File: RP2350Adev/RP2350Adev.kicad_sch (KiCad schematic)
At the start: 43 parts, among them J1 USB4105-GF-A, J2 LEFT, J3 DEBUG, J4 RIGHT, U1 W25Q32JV, U2 RP2350A, U3 MCP1702T-3302E_CB, X1 IQXO-791

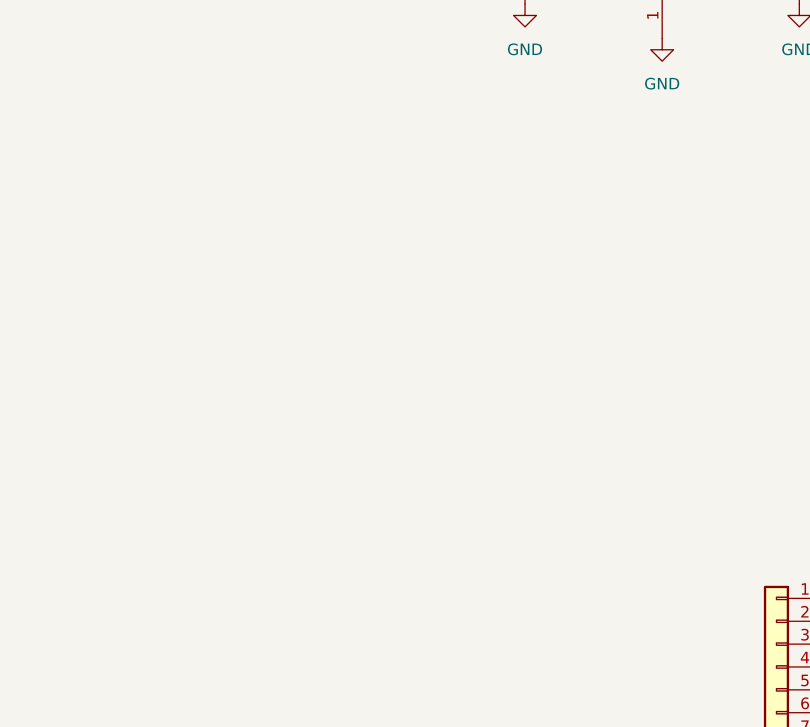
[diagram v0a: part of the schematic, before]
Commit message: add nrf70
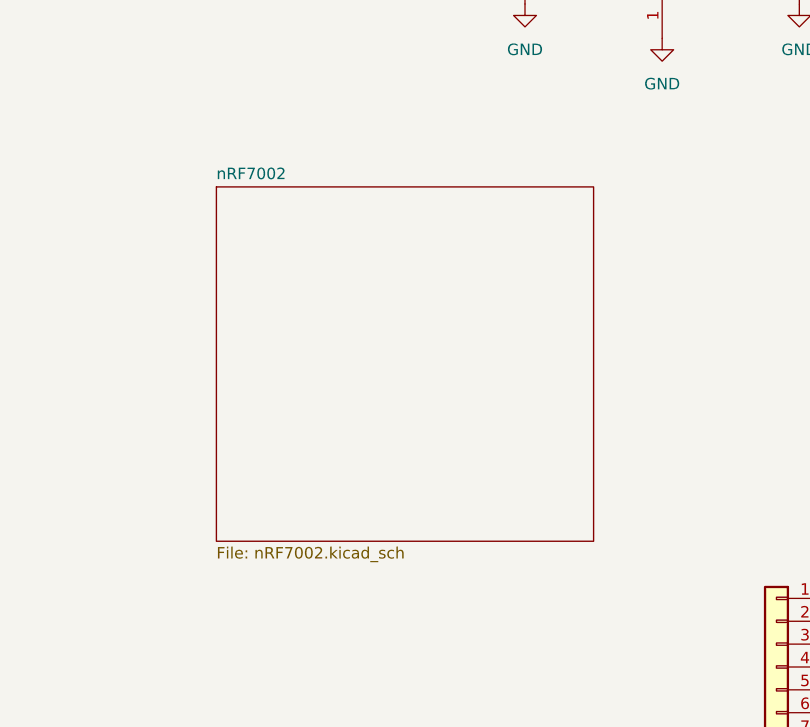
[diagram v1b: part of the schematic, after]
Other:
- added sheet nRF7002 (nRF7002.kicad_sch)
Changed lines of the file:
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@@
+		)
+	)
+	(sheet
+		(at 204.47 64.77)
+		(size 41.91 39.37)
+		(exclude_from_sim no)
+		(in_bom yes)
+		(on_board yes)
+		(dnp no)
+		(fields_autoplaced yes)
+		(stroke
+			(width 0.1524)
+			(type solid)
+		)
+		(fill
+			(color 0 0 0 0.0000)
+		)
+		(property "Sheetname" "nRF7002"
+			(at 204.47 64.0584 0)
+			(effects
+				(font
+					(size 1.27 1.27)
+				)
+				(justify left bottom)
+			)
+		)
+		(property "Sheetfile" "nRF7002.kicad_sch"
+			(at 204.47 104.7246 0)
+			(effects
+				(font
+					(size 1.27 1.27)
+				)
+				(justify left top)
+			)
+		)
+		(instances
+			(project "RP2350Adev"
+				(path "/4930e8a3-0a58-4861-9c4c-0d8b2139987a"
+					(page "2")
+				)
+			)
 		)
 	)

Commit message: Muxful beginnings
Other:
- moved on the sheet: C16, C17, D3, J2, R12, U3

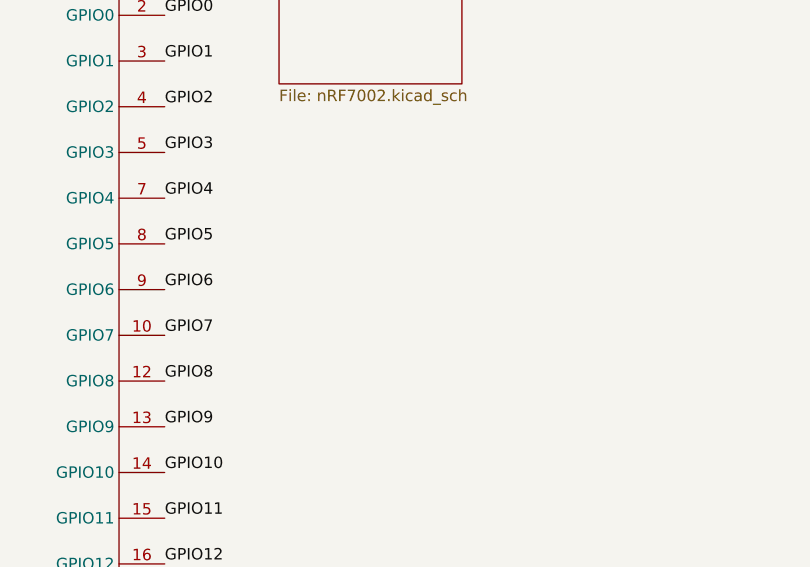
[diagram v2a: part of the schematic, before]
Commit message: link hierarchical sheet and switch from QSPI to SPI
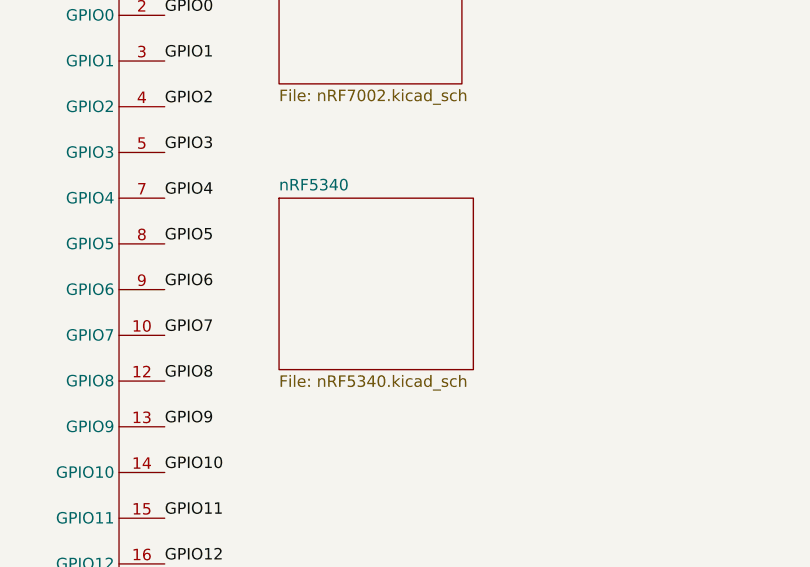
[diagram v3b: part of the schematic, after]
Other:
- added sheet nRF5340 (nRF5340.kicad_sch)
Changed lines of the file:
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@@
+		)
+	)
+	(sheet
+		(at 186.69 53.34)
+		(size 21.59 19.05)
+		(exclude_from_sim no)
+		(in_bom yes)
+		(on_board yes)
+		(dnp no)
+		(fields_autoplaced yes)
+		(stroke
+			(width 0.1524)
+			(type solid)
+		)
+		(fill
+			(color 0 0 0 0.0000)
+		)
+		(property "Sheetname" "nRF5340"
+			(at 186.69 52.6284 0)
+			(effects
+				(font
+					(size 1.27 1.27)
+				)
+				(justify left bottom)
+			)
+		)
+		(property "Sheetfile" "nRF5340.kicad_sch"
+			(at 186.69 72.9746 0)
+			(effects
+				(font
+					(size 1.27 1.27)
+				)
+				(justify left top)
+			)
+		)
+		(instances
+			(project "RP2350Adev"
+				(path "/4930e8a3-0a58-4861-9c4c-0d8b2139987a"
+					(page "3")
+				)
+			)
 		)
 	)

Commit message: Muxful Developings
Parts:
- removed J1: USB4105-GF-A, Eclectronics:USB4105-GF-A, symbol Eclectronics:USB4105-GF-A
- removed R3, R4: 5.1K, Resistor_SMD:R_0402_1005Metric, symbol Device:R
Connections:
- no-connect marks 4 -> 2

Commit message: Combine subsheets
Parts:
- removed J2: LEFT, Connector_PinHeader_2.54mm:PinHeader_1x20_P2.54mm_Vertical, symbol Connector_Generic:Conn_01x20
- removed J4: RIGHT, Connector_PinHeader_2.54mm:PinHeader_1x20_P2.54mm_Vertical, symbol Connector_Generic:Conn_01x20
- added J5: UART, Connector_PinHeader_1.00mm:PinHeader_1x03_P1.00mm_Vertical, symbol Connector_Generic:Conn_01x03
- renumbered C16 to C26, C1 to C27, C17 to C28, C2 to C29, C3 to C30, C4 to C31, C5 to C32, C6 to C33, C7 to C34, C8 to C35, C9 to C36, C10 to C37, C11 to C38, C12 to C39, C13 to C40, C14 to C41, C15 to C42, D3 to D2, D1 to D3, D2 to D4, J3 to J6, L1 to L7, R12 to R10, R5 to R11, R6 to R12, R7 to R13, R8 to R14, R9 to R15, R10 to R16, R11 to R17, R1 to R8, R2 to R9, U3 to U5, U1 to U6, U2 to U7, X1 to X4
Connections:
- net GND: now also J5.3 (Pin_3)
- net D1+: now reaches R12.1
- net D1-: now reaches R11.1
- net GPIO0: no longer names the net of U7.2 (GPIO0)
- net GPIO0: now also J5.1 (Pin_1)
- net GPIO1: no longer names the net of U7.3 (GPIO1)
- net GPIO1: now also J5.2 (Pin_2)
- net GPIO10 renamed MUX2_S
- net GPIO11 renamed MUX2_OE
- net GPIO12 renamed MUX1_S1
- net GPIO13 renamed MUX1_S0
- net GPIO14 renamed D2+
- net GPIO15 renamed D2-
- net GPIO2 renamed SPI_CLK
- net GPIO3 renamed SPI_MOSI
- net GPIO4 renamed SPI_MISO
- net GPIO5 renamed SPI_SS
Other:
- removed sheet nRF5340
- removed sheet nRF7002
- company: Olin College -> (none)
- title: RP2350A Development Board -> (none)
- moved on the sheet: J6

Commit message: Layout Assembly Attempt (Components not being transferred as expected, major issues)
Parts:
- renumbered C26 to C36, C27 to C37, C28 to C38, C29 to C39, C30 to C40, C31 to C41, C32 to C42, C33 to C43, C34 to C44, C35 to C45, C36 to C46, C37 to C47, C38 to C48, C39 to C49, C40 to C50, C41 to C51, C42 to C52
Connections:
- no-connect marks 2 -> 16

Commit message: Combine subcircuits
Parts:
- J401: renamed from J5; footprint Connector_PinHeader_1.00mm:PinHeader_1x03_P1.00mm_Vertical -> Connector_PinHeader_2.54mm:PinHeader_1x03_P2.54mm_Vertical
- J402: renamed from J6; footprint Connector_PinHeader_1.00mm:PinHeader_1x03_P1.00mm_Vertical -> Connector_PinHeader_2.54mm:PinHeader_1x03_P2.54mm_Vertical
- U401: renamed from U5; footprint Parts:SOT95P255X145-3N -> Package_TO_SOT_SMD:SOT-23
- renumbered C36 to C401, C37 to C402, C38 to C403, C39 to C404, C40 to C405, C41 to C406, C42 to C407, C43 to C408, C44 to C409, C45 to C410, C46 to C411, C47 to C412, C48 to C413, C49 to C414, C50 to C415, C51 to C416, C52 to C417, D2 to D401, D3 to D402, D4 to D403, L7 to L401, R8 to R401, R9 to R402, R10 to R403, R11 to R404, R12 to R405, R13 to R406, R14 to R407, R15 to R408, R16 to R409, R17 to R410, S1 to S401, S2 to S402, U6 to U402, U7 to U403, X4 to X401
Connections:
- net GPIO6 is gone; now on net MUX2_S: U403.9 (GPIO6)
- net GPIO7 is gone; now on net MUX2_OE: U403.10 (GPIO7)
- net GPIO8 is gone; now on net MUX1_S1: U403.12 (GPIO8)
- net GPIO9 is gone; now on net MUX1_S0: U403.13 (GPIO9)
- net MUX1_S0: no longer U403.17 (GPIO13)
- net MUX1_S1: no longer U403.16 (GPIO12)
- net MUX2_OE: no longer U403.15 (GPIO11)
- net MUX2_S: no longer U403.14 (GPIO10)
- net GPIO16 renamed HOST_IRQ
- net GPIO17 renamed BUCK_EN
- net GPIO18 renamed IOVDD_EN
- new net SPI_CLK2: U403.14 (GPIO10)
- new net SPI_MISO2: U403.16 (GPIO12)
- new net SPI_MOSI2: U403.15 (GPIO11)
- new net SPI_SS2: U403.17 (GPIO13)
- no-connect marks 16 -> 9
